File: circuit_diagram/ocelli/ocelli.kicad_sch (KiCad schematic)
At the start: 114 parts, among them J1 Conn_01x06, J2 Conn_01x06, J3 Conn_01x06, J4 Conn_01x06, J5 Conn_01x08, J6 Conn_01x02, J7 Conn_01x02, Q1 BSS138, Q10 BSS138, Q2 ST-1KL3A, Q3 TJ8S06M3L, Q4 ST-1KL3A, Q5 BSS138, Q6 ST-1KL3A, Q7 BSS138, Q8 ST-1KL3A, Q9 BSS138, SW1 SW_SPDT, SW2 TS-06104, SW3 TS-06104, SW4 TS-06104, SW5 SW_Push, SW6 SW_Push, U1 NJM2845DL1-33, U2 AS5055A, U3 AS5055A, U4 ICM-20649, U5 STM32F405RGTx, U6 DRV8835

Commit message: 抵抗の選定
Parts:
- C1, C10, C13, C25, C5: value 0.01u 10V 5% -> 0.01u 5%
- C11, C12, C14, C15, C16, C18, C21, C22, C23, C24, C26, C29, C3, C30, C31, C4: value 0.1u 10V 10% -> 0.1u
- C17, C19, C9: value 2.2u 6.3V 10% -> 2.2u; url https://www.digikey.jp/ja/products/detail/taiyo-yuden/JMK10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 -> https://www.digikey.jp/ja/products/detail/taiyo-yuden/LMK10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
- C20, C7, C8: value 4.7u 6.3V 10% -> 4.7u; url https://www.digikey.jp/ja/products/detail/taiyo-yuden/JMK10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 -> https://www.digikey.jp/ja/products/detail/taiyo-yuden/LMK10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
- C27: value 1u 6.3V 10% -> 1u; url https://www.digikey.jp/ja/products/detail/taiyo-yuden/JMK10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 -> https://www.digikey.jp/ja/products/detail/taiyo-yuden/LMK10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
- C28: value 10u 10V 10% -> 10u
- C6: value 1u 10V 10% -> 1u
- R1, R10, R11, R12, R13, R15, R16, R17, R18, R2, R22, R23, R24, R25, R26, R27, R28, R30, R31, R32, R33, R34, R35, R36, R37, R38, R39, R4, R41, R42, R5, R6, R7, R8, R9: url (none) -> https://www.digikey.jp/ja/products/detail/koa-speer-electro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
- R14, R19, R20, R21, R29, R3: url (none) -> https://www.digikey.jp/ja/products/detail/bourns-inc/CR0603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
- RV1: value 10k -> 10k 1/4W 20%; url (none) -> https://www.digikey.jp/ja/products/detail/nidec-copal-elect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
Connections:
- net +3.3V: now also C30.2, R5.2, R6.2; no longer C30.1, R5.1, R6.1
- net +BATT: now also C28.2, C29.2; no longer C28.1, C29.1
- net GND: now also C28.1, C29.1, C30.1, R12.2, R17.2, R2.2, R26.2; no longer C28.2, C29.2, C30.2, R12.1, R17.1, R2.1, R26.1
- net LEFT_FRONT_IR: now also R25.2; no longer R25.1
- net LEFT_SIDE_IR: now also R11.1; no longer R11.2
- net RIGHT_FRONT_IR: now also R16.2; no longer R16.1
- net RIGHT_SIDE_IR: now also R1.1; no longer R1.2
- net SPI2_CS0: now also R5.1; no longer R5.2
- net SPI2_CS1: now also R6.1; no longer R6.2
- net VDD_L: now also R19.2; no longer R19.1
- net VDD_R: now also R20.2; no longer R20.1
- net at C8.2, U3.12 (VDD): now also R20.1; no longer R20.2
- net at C7.2, U2.12 (VDD): now also R19.1; no longer R19.2
- net at Q3.1 (G), SW1.2 (B): now also R7.1; no longer R7.2
- net at BT1.1 (+), Q3.3 (S): now also R7.2; no longer R7.1
- new net: Q7.1 (G), R16.1, R17.1
- new net: Q9.1 (G), R25.1, R26.1
- new net: Q1.1 (G), R1.2, R2.1
- new net: Q5.1 (G), R11.2, R12.1
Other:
- note added: "表記のない抵抗の定格電力、許容誤差は1/10W、±1% 表記のないコンデンサの耐圧、許容誤差は10V、±10%"
- moved on the sheet: BT1, C2, C20, C21, C22, C23, C24, C28, C29, C3, C30, C31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

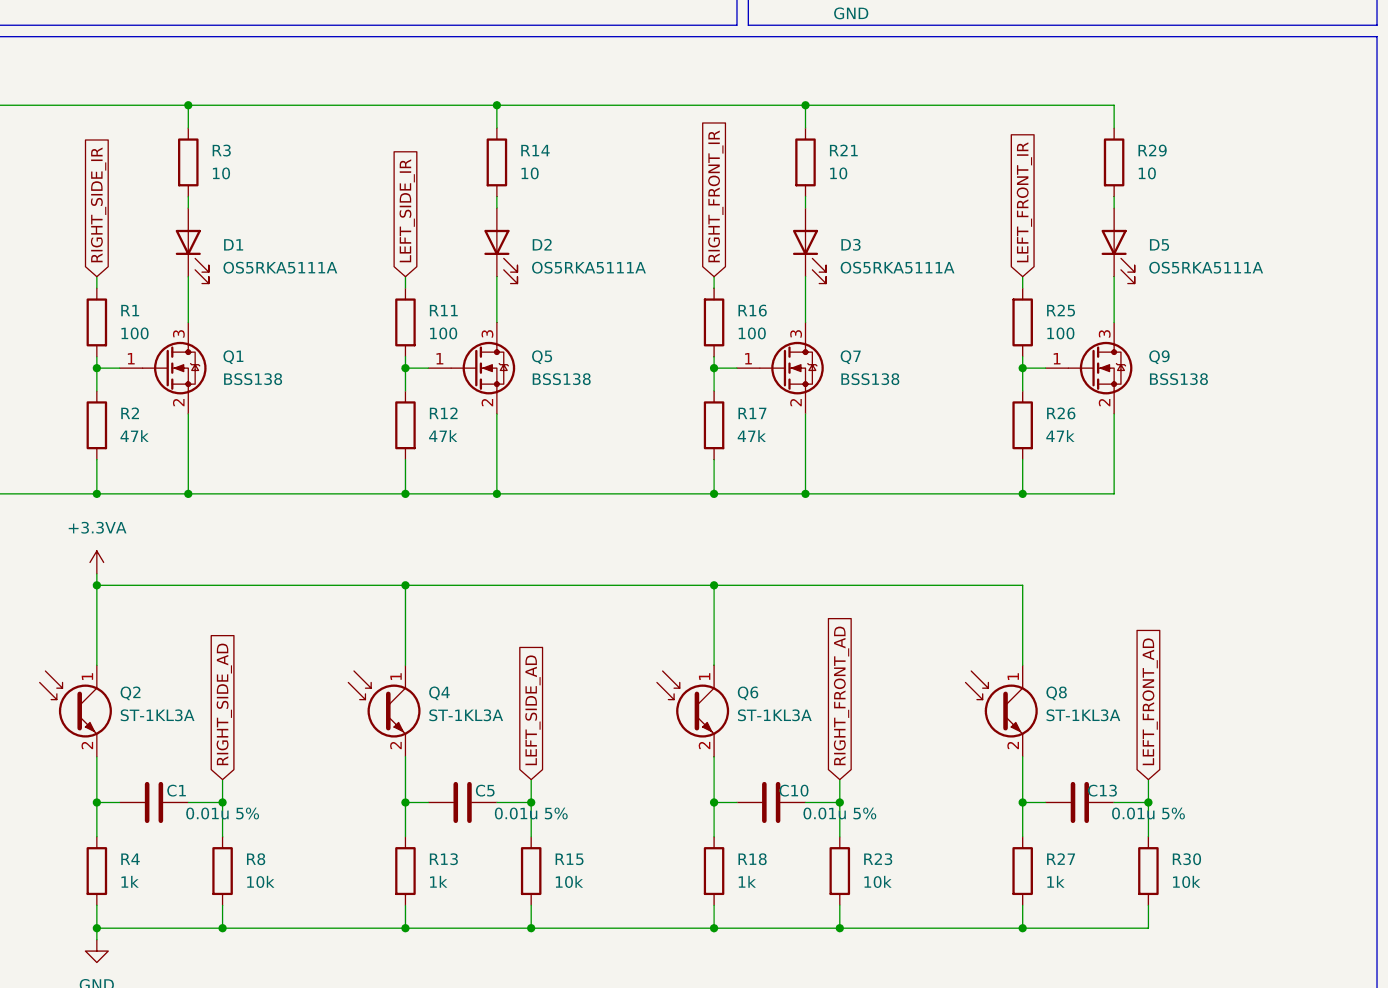
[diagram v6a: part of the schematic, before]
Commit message: 距離センサ用抵抗の定格電力修正
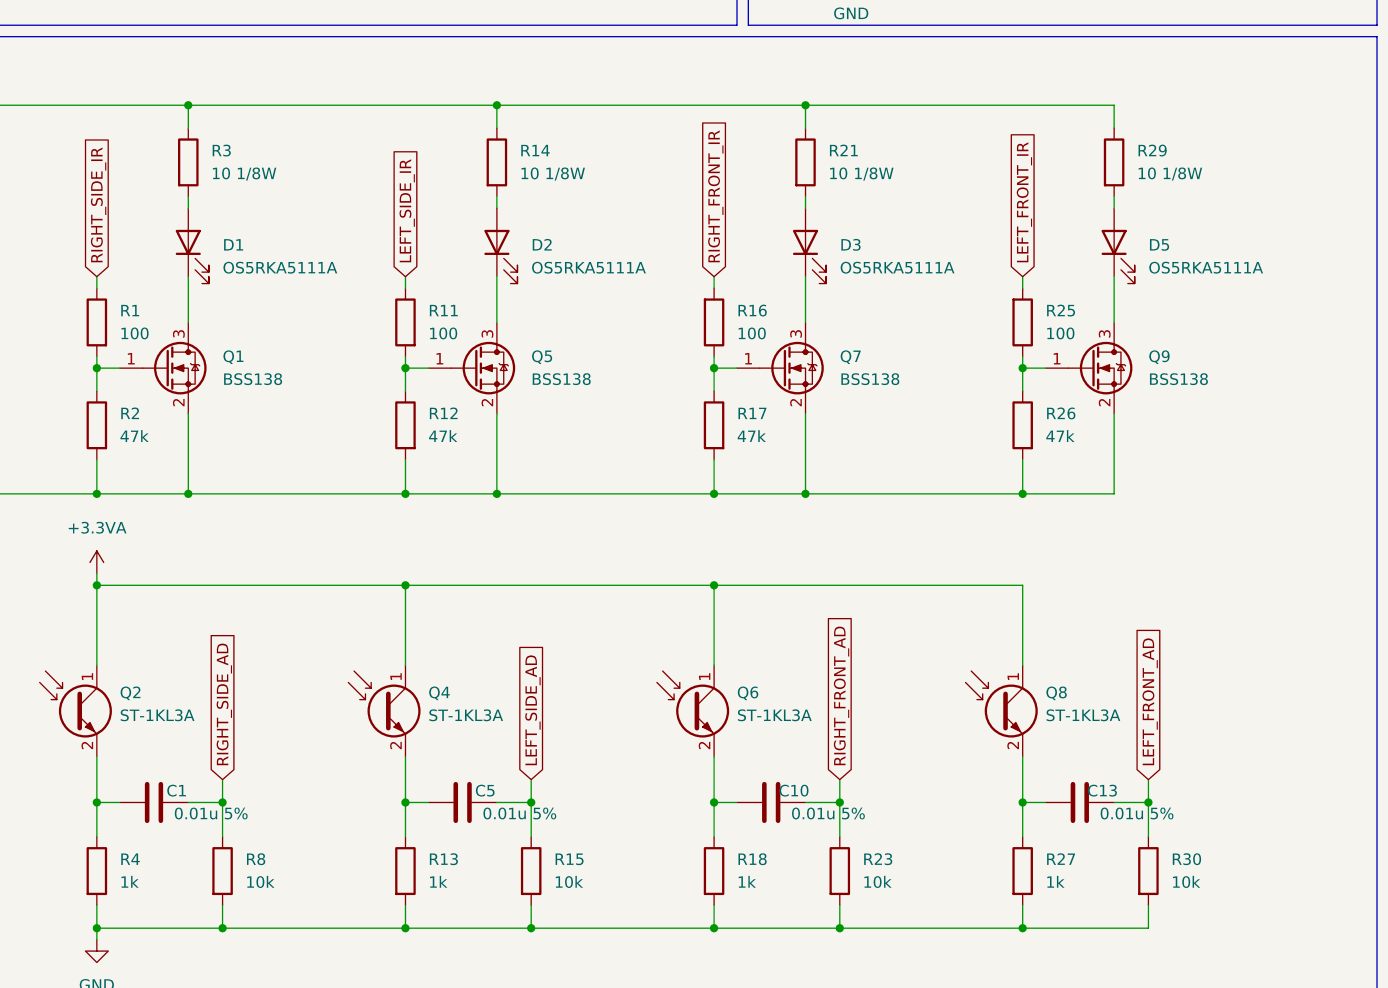
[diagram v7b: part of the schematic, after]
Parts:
- R14, R21, R29, R3: value 10 -> 10 1/8W; url https://www.digikey.jp/ja/products/detail/bourns-inc/CR0603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 -> https://www.digikey.jp/ja/products/detail/koa-speer-electro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
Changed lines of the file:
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@@
     (in_bom yes) (on_board yes)
     (property "Reference" "C10" (id 0) (at 135.89 146.05 90))
-    (property "Value" "0.01u 5%" (id 1) (at 140.97 148.59 90))
+    (property "Value" "0.01u 5%" (id 1) (at 139.7 148.59 90))
     (property "Footprint" "" (id 2) (at 137.16 146.3548 0)
       (effects (font (size 1.27 1.27)) hide)
@@
     (in_bom yes) (on_board yes)
     (property "Reference" "C13" (id 0) (at 170.18 146.05 90))
-    (property "Value" "0.01u 5%" (id 1) (at 175.26 148.59 90))
+    (property "Value" "0.01u 5%" (id 1) (at 173.99 148.59 90))
     (property "Footprint" "" (id 2) (at 171.45 146.3548 0)
       (effects (font (size 1.27 1.27)) hide)
@@
     (in_bom yes) (on_board yes)
     (property "Reference" "C1" (id 0) (at 67.31 146.05 90))
-    (property "Value" "0.01u 5%" (id 1) (at 72.39 148.59 90))
+    (property "Value" "0.01u 5%" (id 1) (at 71.12 148.59 90))
     (property "Footprint" "" (id 2) (at 68.58 146.3548 0)
       (effects (font (size 1.27 1.27)) hide)
@@
       (effects (font (size 1.27 1.27)) (justify left))
     )
-    (property "Value" "10" (id 1) (at 71.12 77.4699 0)
+    (property "Value" "10 1/8W" (id 1) (at 71.12 77.4699 0)
       (effects (font (size 1.27 1.27)) (justify left))
     )
@@
       (effects (font (size 1.27 1.27)) hide)
     )
-    (property "url" "https://www.digikey.jp/ja/products/detail/bourns-inc/CR0603-FX-10R0ELF/3740906" (id 4) (at 68.58 76.2 0)
+    (property "url" "https://www.digikey.jp/ja/products/detail/koa-speer-electronics-inc/RK73H1JRTTD10R0F/12314770" (id 4) (at 68.58 76.2 0)
       (effects (font (size 1.27 1.27)) hide)
     )
@@
       (effects (font (size 1.27 1.27)) (justify left))
     )
-    (property "Value" "10" (id 1) (at 105.41 77.4699 0)
+    (property "Value" "10 1/8W" (id 1) (at 105.41 77.4699 0)
       (effects (font (size 1.27 1.27)) (justify left))
     )
@@
       (effects (font (size 1.27 1.27)) hide)
     )
-    (property "url" "https://www.digikey.jp/ja/products/detail/bourns-inc/CR0603-FX-10R0ELF/3740906" (id 4) (at 102.87 76.2 0)
+    (property "url" "https://www.digikey.jp/ja/products/detail/koa-speer-electronics-inc/RK73H1JRTTD10R0F/12314770" (id 4) (at 102.87 76.2 0)
       (effects (font (size 1.27 1.27)) hide)
     )
@@
     (in_bom yes) (on_board yes)
     (property "Reference" "C5" (id 0) (at 101.6 146.05 90))
-    (property "Value" "0.01u 5%" (id 1) (at 106.68 148.59 90))
+    (property "Value" "0.01u 5%" (id 1) (at 105.41 148.59 90))
     (property "Footprint" "" (id 2) (at 102.87 146.3548 0)
       (effects (font (size 1.27 1.27)) hide)
@@
       (effects (font (size 1.27 1.27)) (justify left))
     )
-    (property "Value" "10" (id 1) (at 139.7 77.4699 0)
+    (property "Value" "10 1/8W" (id 1) (at 139.7 77.4699 0)
       (effects (font (size 1.27 1.27)) (justify left))
     )
@@
       (effects (font (size 1.27 1.27)) hide)
     )
-    (property "url" "https://www.digikey.jp/ja/products/detail/bourns-inc/CR0603-FX-10R0ELF/3740906" (id 4) (at 137.16 76.2 0)
+    (property "url" "https://www.digikey.jp/ja/products/detail/koa-speer-electronics-inc/RK73H1JRTTD10R0F/12314770" (id 4) (at 137.16 76.2 0)
       (effects (font (size 1.27 1.27)) hide)
     )
@@
       (effects (font (size 1.27 1.27)) (justify left))
     )
-    (property "Value" "10" (id 1) (at 173.99 77.4699 0)
+    (property "Value" "10 1/8W" (id 1) (at 173.99 77.4699 0)
       (effects (font (size 1.27 1.27)) (justify left))
     )
@@
       (effects (font (size 1.27 1.27)) hide)
     )
-    (property "url" "https://www.digikey.jp/ja/products/detail/bourns-inc/CR0603-FX-10R0ELF/3740906" (id 4) (at 171.45 76.2 0)
+    (property "url" "https://www.digikey.jp/ja/products/detail/koa-speer-electronics-inc/RK73H1JRTTD10R0F/12314770" (id 4) (at 171.45 76.2 0)
       (effects (font (size 1.27 1.27)) hide)
     )
@@
     )
     (path "/40dea6ce-790b-47ac-afa8-5f5714d006b6"
-      (reference "R3") (unit 1) (value "10") (footprint "")
+      (reference "R3") (unit 1) (value "10 1/8W") (footprint "")
     )
     (path "/f0c6c69e-8789-4048-b350-cea39d346d01"
@@
     )
     (path "/8418d2a5-e4c9-4427-9ad0-cda6ada6602c"
-      (reference "R14") (unit 1) (value "10") (footprint "")
+      (reference "R14") (unit 1) (value "10 1/8W") (footprint "")
     )
     (path "/3d55f8a8-2118-482d-a00a-df7a6de94883"
@@
     )
     (path "/ac6aa813-d93d-4468-abb4-f60b919ee5f2"
-      (reference "R21") (unit 1) (value "10") (footprint "")
+      (reference "R21") (unit 1) (value "10 1/8W") (footprint "")
     )
     (path "/28bbea58-87b9-4a40-9a8c-50a49711fa9c"
@@
     )
     (path "/fc53bc3e-5430-47a9-a604-3bf3c4193aee"
-      (reference "R29") (unit 1) (value "10") (footprint "")
+      (reference "R29") (unit 1) (value "10 1/8W") (footprint "")
     )
     (path "/27b90acc-c409-469b-89a6-4cbec994a07a"

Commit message: フットプリント追加
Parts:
- C1, C10, C11, C12, C13, C14, C15, C16, C17, C18, C19, C20, C21, C22, C23, C24, C25, C26, C27, C28, C29, C3, C30, C31, C4, C5, C6, C7, C8, C9: footprint (none) -> Capacitor_SMD:C_0603_1608Metric_Pad1.08x0.95mm_HandSolder
- D4, D6, D7, D8, D9: footprint (none) -> LED_SMD:LED_0603_1608Metric_Pad1.05x0.95mm_HandSolder
- R1, R10, R11, R12, R13, R14, R15, R16, R17, R18, R19, R2, R20, R21, R22, R23, R24, R25, R26, R27, R28, R29, R3, R30, R31, R32, R33, R34, R35, R36, R37, R38, R39, R4, R41, R42, R5, R6, R7, R8, R9: footprint (none) -> Resistor_SMD:R_0603_1608Metric_Pad0.98x0.95mm_HandSolder
